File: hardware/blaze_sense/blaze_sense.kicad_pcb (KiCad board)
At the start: 4 copper layers, 70 x 70 mm, 81 parts, among them J1 FrontInterconnect, J2 RearInterconnect, P1 TC2030-CTX, SW1 SW_SPST, SW2 SW_SPDT, U1 ADXL375, U1 TCAN1044VDDFR, U2 BMI088, U3 A3G4250D, U4 ADXL345, U5 MS5611-01BA, U6 RM3100, U8 TCAN1044VDDFR, U9 STM32H523RET6, Y1 ABM3-8.000MHZ-B4Y-T, Y2 ABS07-32.768KHZ-T

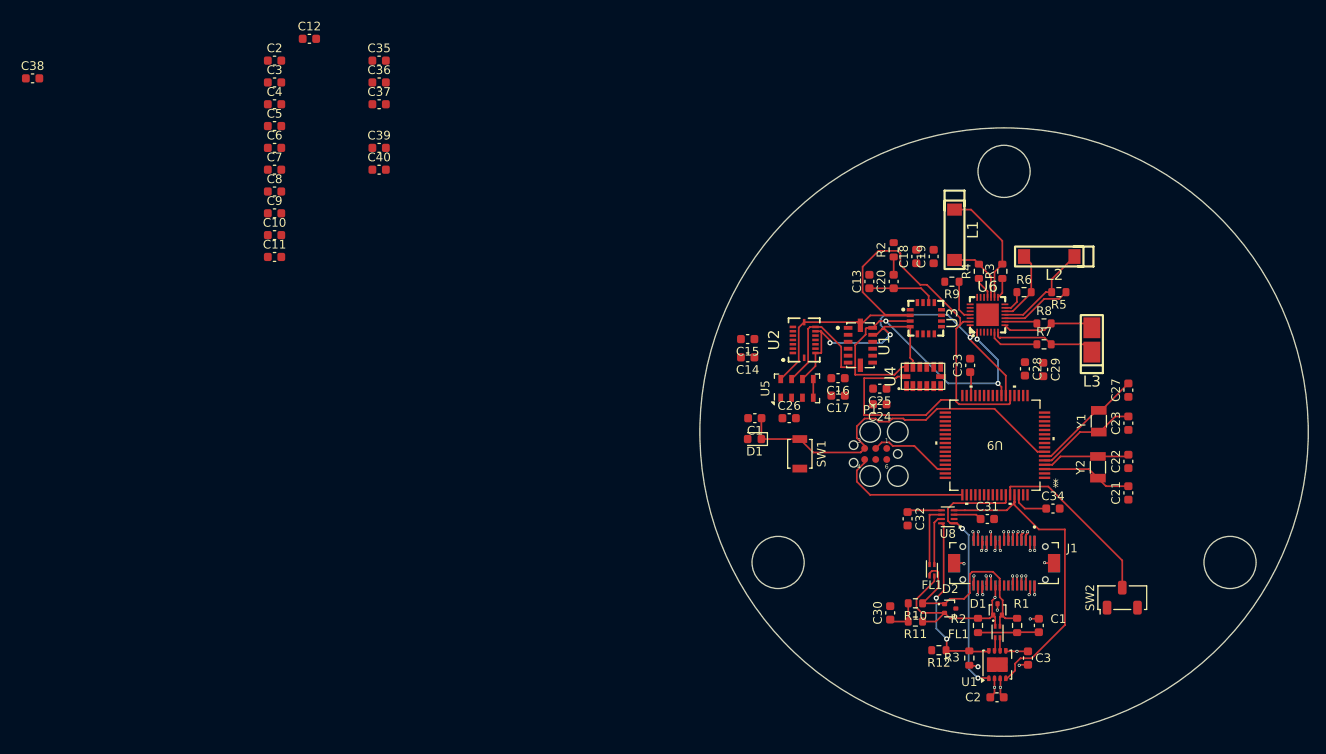
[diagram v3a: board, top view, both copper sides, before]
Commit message: Removed redundant CAN footprints
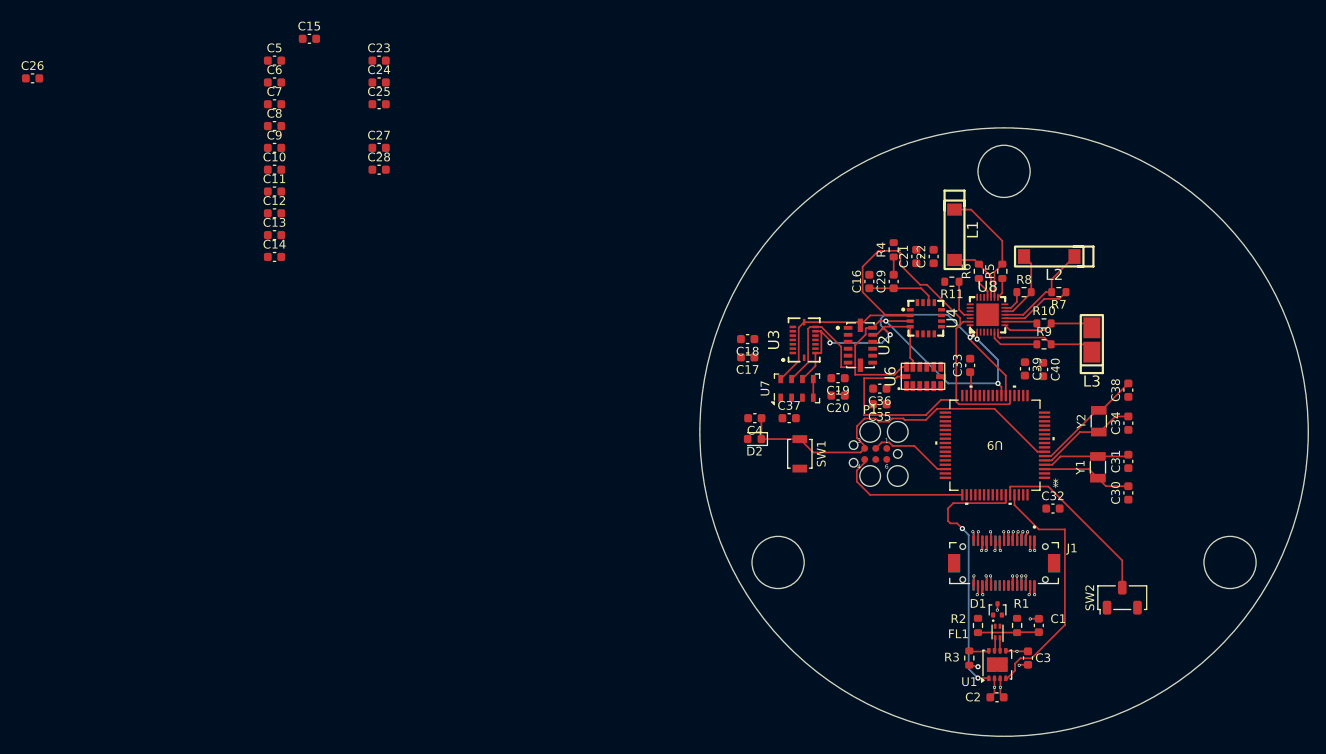
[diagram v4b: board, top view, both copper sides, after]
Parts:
- removed the C30 at (135.4, 126.3)
- removed the C31 at (146.6, 115.5)
- removed the C32 at (137.4, 115.5)
- removed the D2 at (142.3, 125.8)
- removed the FL1 at (140.2, 121.4)
- removed the R10 at (138.3, 125.2)
- removed the R11 at (138.3, 127.3)
- removed R12: 10K, Resistor_SMD:R_0603_1608Metric
- removed the U8 at (142.0, 115.2)
- J1: value FrontInterconnect -> Conn_01x30_Pin
- J2: value RearInterconnect -> Conn_01x30_Socket
- renumbered C7 to C10, C8 to C11, C9 to C12, C10 to C13, C11 to C14, C12 to C15, C13 to C16, C14 to C17, C15 to C18, C16 to C19, C17 to C20, C18 to C21, C19 to C22, C35 to C23, C36 to C24, C37 to C25, C38 to C26, C39 to C27, C40 to C28, C20 to C29, C21 to C30, C22 to C31, C34 to C32, C23 to C34, C24 to C35, C25 to C36, C26 to C37, C27 to C38, C28 to C39, C1 to C4, C29 to C40, C2 to C5, C3 to C6, C4 to C7, C5 to C8, C6 to C9, D1 to D2, R8 to R10, R9 to R11, R2 to R4, R3 to R5, R4 to R6, R5 to R7, R6 to R8, R7 to R9, U1 to U2, U2 to U3, U3 to U4, U4 to U6, U5 to U7, U6 to U8, Y2 to Y1, Y1 to Y2
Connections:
- C32 pad 1: Net-(C34-Pad1) -> Net-(C32-Pad1)
- D1 pad 1: /CANH -> /CANL
- D1 pad 2: /CANL -> /CANH
- J1 pad 21: /CANH -> /CANL
- J1 pad 22: /CANL -> /CANH
- J1 pad S1: GND -> (no net)
- J1 pad S2: GND -> (no net)
- J2 pad 10: /CANH -> /CANL
- J2 pad 9: /CANL -> /CANH
- J2 pad S1: GND -> (no net)
- J2 pad S2: GND -> (no net)
- U9 pad 38: unconnected-(U9A-PC7-Pad38) -> (no net)
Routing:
- net /CANL: track 25.5 -> 0.00 mm
- net /CANH: track 21.9 -> 0.00 mm, vias 1 -> 0
- net /CAN_STB: track 20.6 -> 2.27 mm, vias 2 -> 0
- net /CANRX: track 36.4 -> 29.0 mm
- net Net-(U8-CANL): track 7.12 -> 0.00 mm
- net Net-(U8-CANH): track 5.83 -> 0.00 mm
- net GND: track 23.2 -> 18.7 mm, vias 12 -> 10
- net Net-(C34-Pad1): track 4.33 -> 0.00 mm
- net Net-(C30-Pad1): track 4.27 -> 0.00 mm
- net +3V3: track 16.6 -> 12.6 mm
- net +5V: track 29.8 -> 26.6 mm

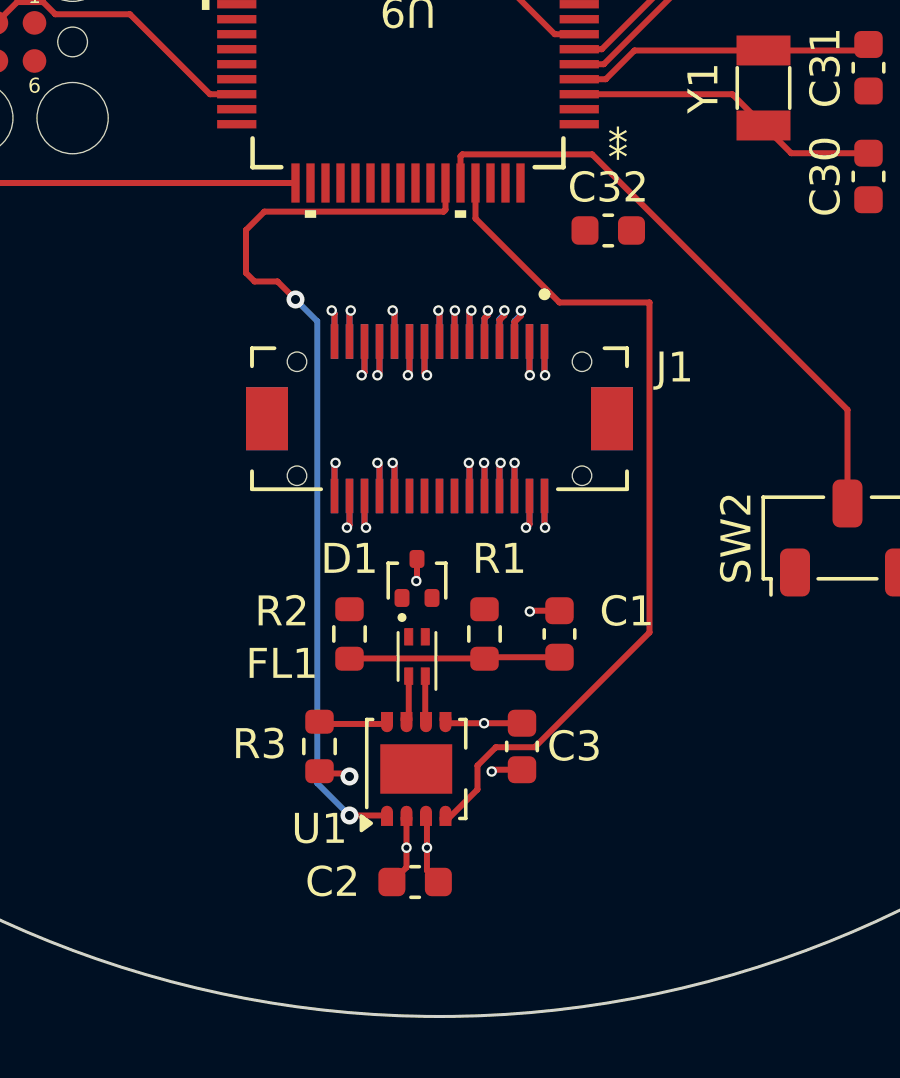
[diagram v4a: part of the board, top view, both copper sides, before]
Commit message: Repaired CAN routing
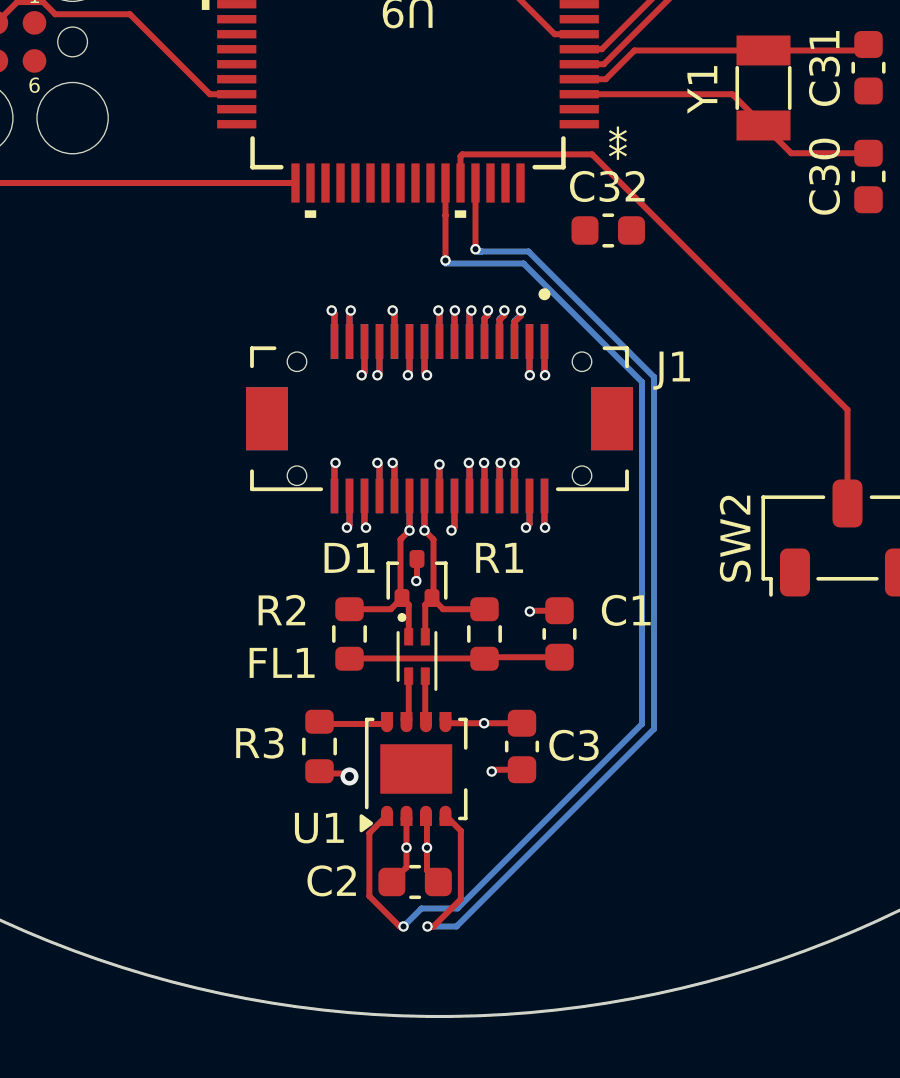
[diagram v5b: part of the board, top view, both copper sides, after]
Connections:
- D1 pad 1: /CANL -> /CANH
- D1 pad 2: /CANH -> /CANL
- J1 pad 21: /CANL -> /CANH
- J1 pad 22: /CANH -> /CANL
- J2 pad 10: /CANL -> /CANH
- J2 pad 9: /CANH -> /CANL
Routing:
- net /CANL: track 0.00 -> 7.99 mm, vias 0 -> 1
- net /CANH: track 0.00 -> 7.99 mm, vias 0 -> 1
- net /CANRX: track 29.0 -> 36.6 mm, vias 0 -> 2
- net /CANTX: track 30.5 -> 37.5 mm
- net Net-(J1-Pin_24): track 0.00 -> 2.38 mm, vias 0 -> 1
- net Net-(J1-Pin_23): track 0.00 -> 2.10 mm, vias 0 -> 1

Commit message: Updated annotation
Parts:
- renumbered U9 to U5
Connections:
- U5 pad 38: (no net) -> unconnected-(U5A-PC7-Pad38)
- U5 pad 62: Net-(C34-Pad1) -> Net-(C32-Pad1)
